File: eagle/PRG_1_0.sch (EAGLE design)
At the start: 15 parts, among them IC1 74HC374N, IC2 74HC86N, X1 Ctrl, X2 Out Serial, X3 Out A, X4 Out B

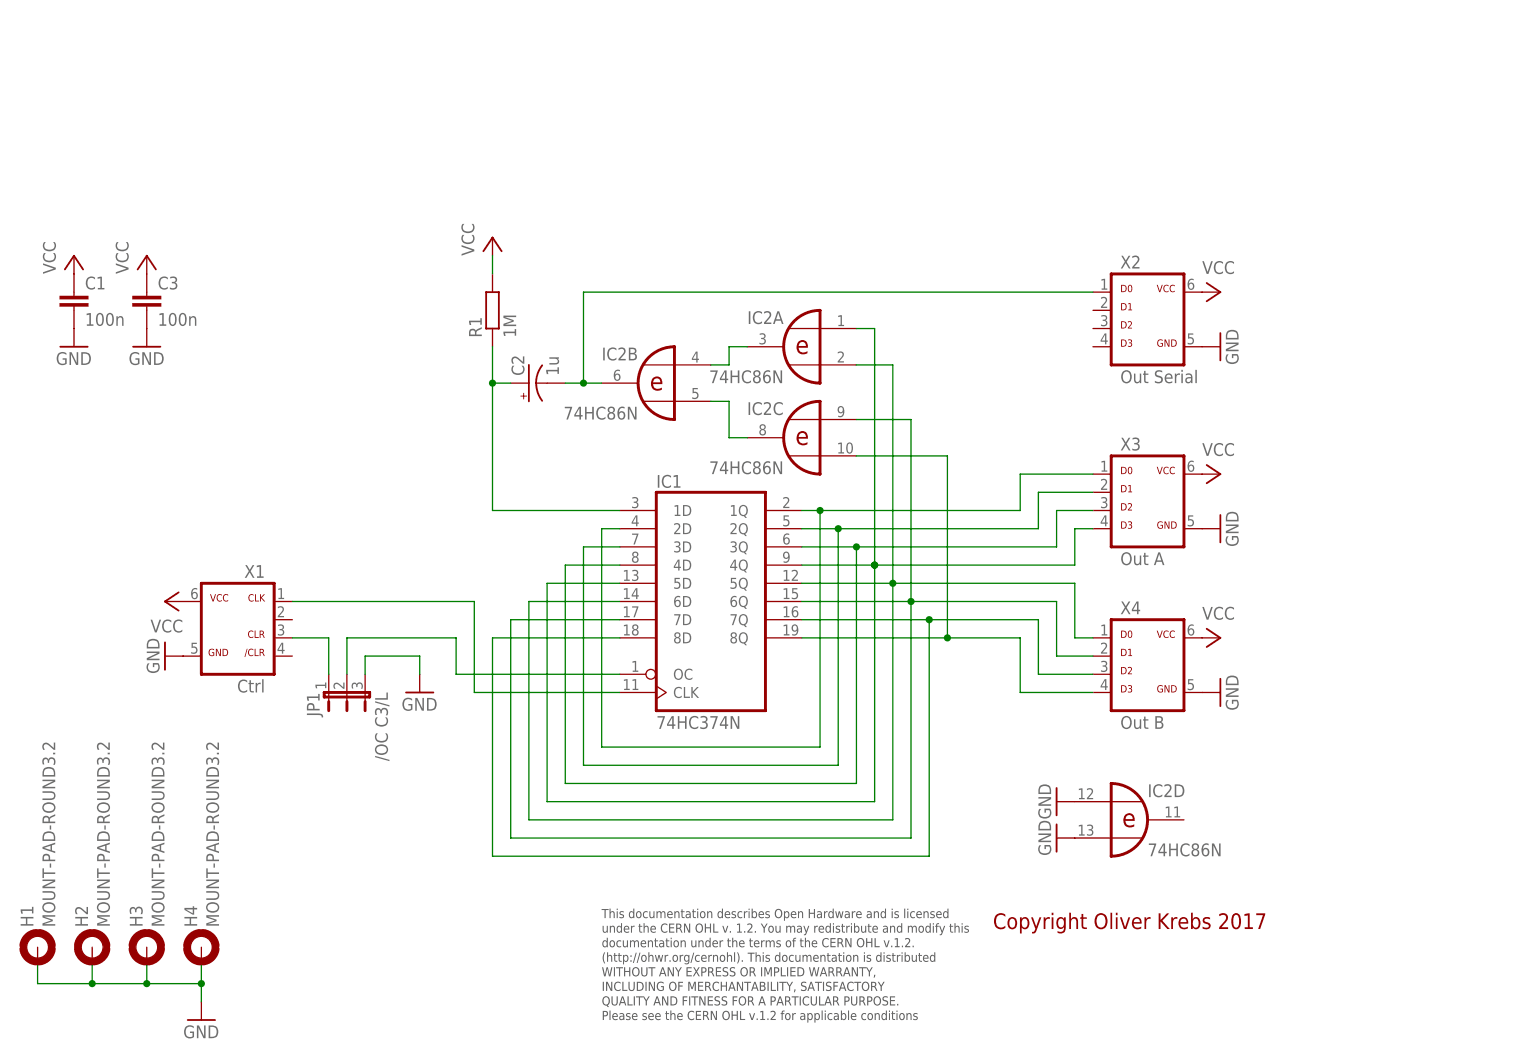
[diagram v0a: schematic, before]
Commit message: Add new tetra-Board and arduino files
Add AMP_1_0, AVC_1_0, D18_1_1, IOP_1_2, MIC_1_0, PIN_1_1, POT_1_0, PWA_1_0, PWR_1_0, RGF 2.0, SOC_2_0, VLT_1_0
Add mex_nano_shield_keyboard, mex_nano_shied_numbers

New arduino projects
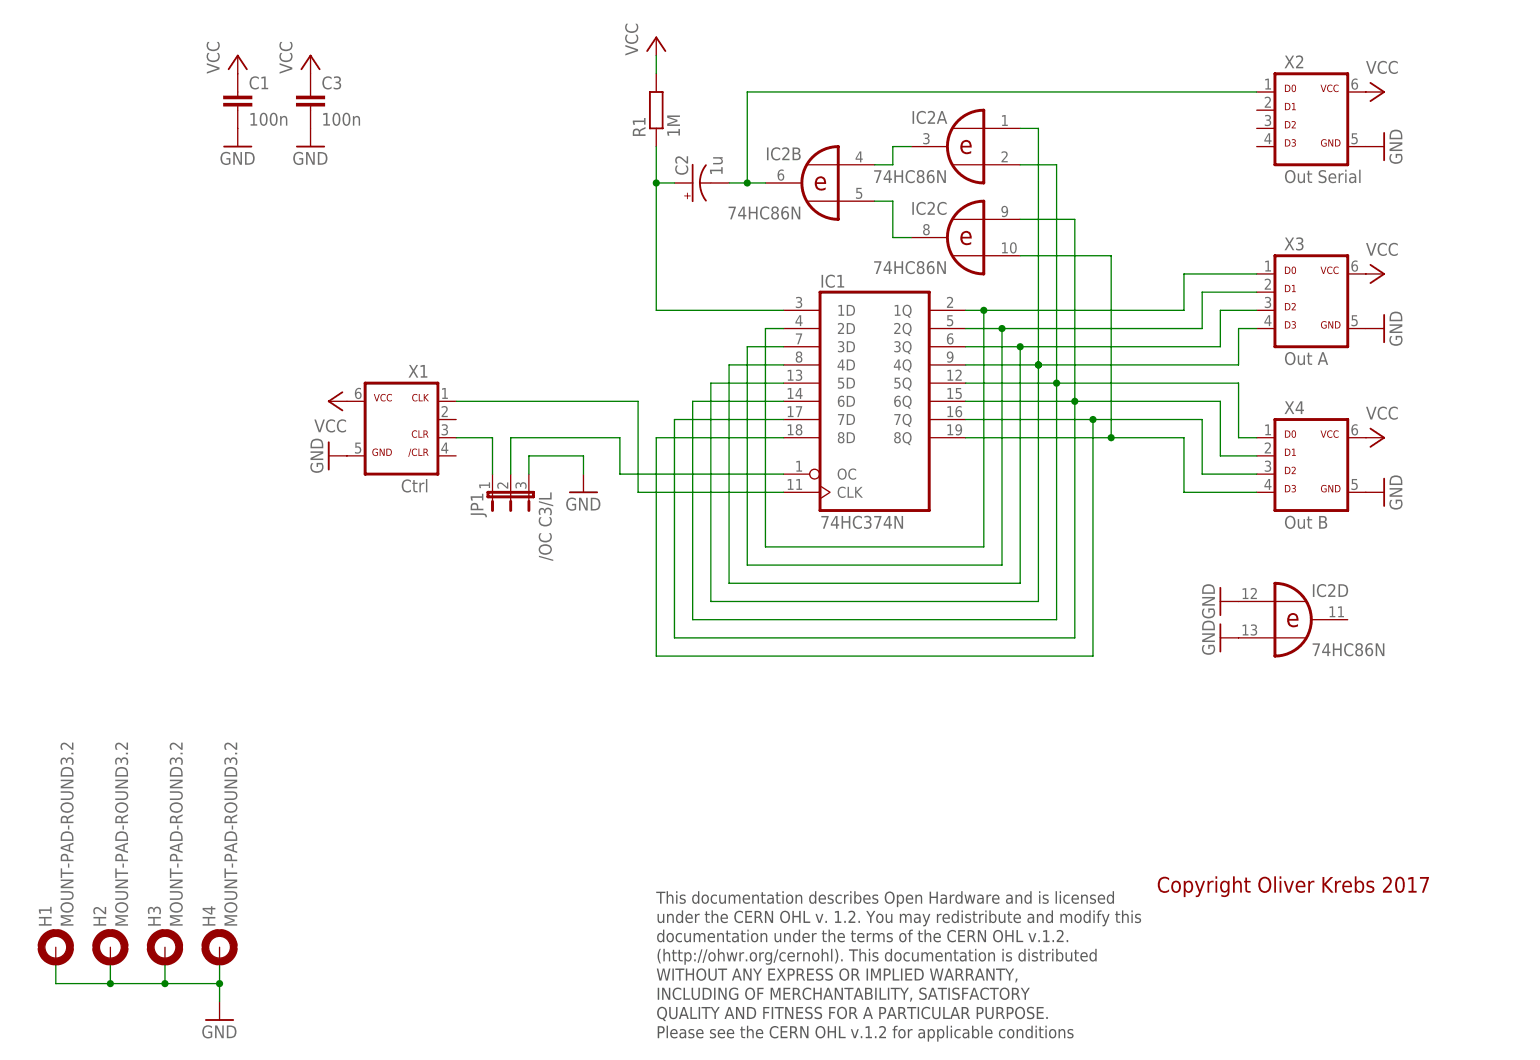
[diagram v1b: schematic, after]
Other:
- moved on the sheet: C1, C2, C3, H1, H2, H3, H4, IC1, IC2A, IC2B, IC2C, IC2D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
